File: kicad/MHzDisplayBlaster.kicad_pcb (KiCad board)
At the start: 2 copper layers, 39.6 x 31.2 mm, 5 parts, among them J1 Conn_02x15 DigitRHS, J2 Conn_02x15 DigitLHS, J4 Conn_01x07, U1 DC56-11GWA

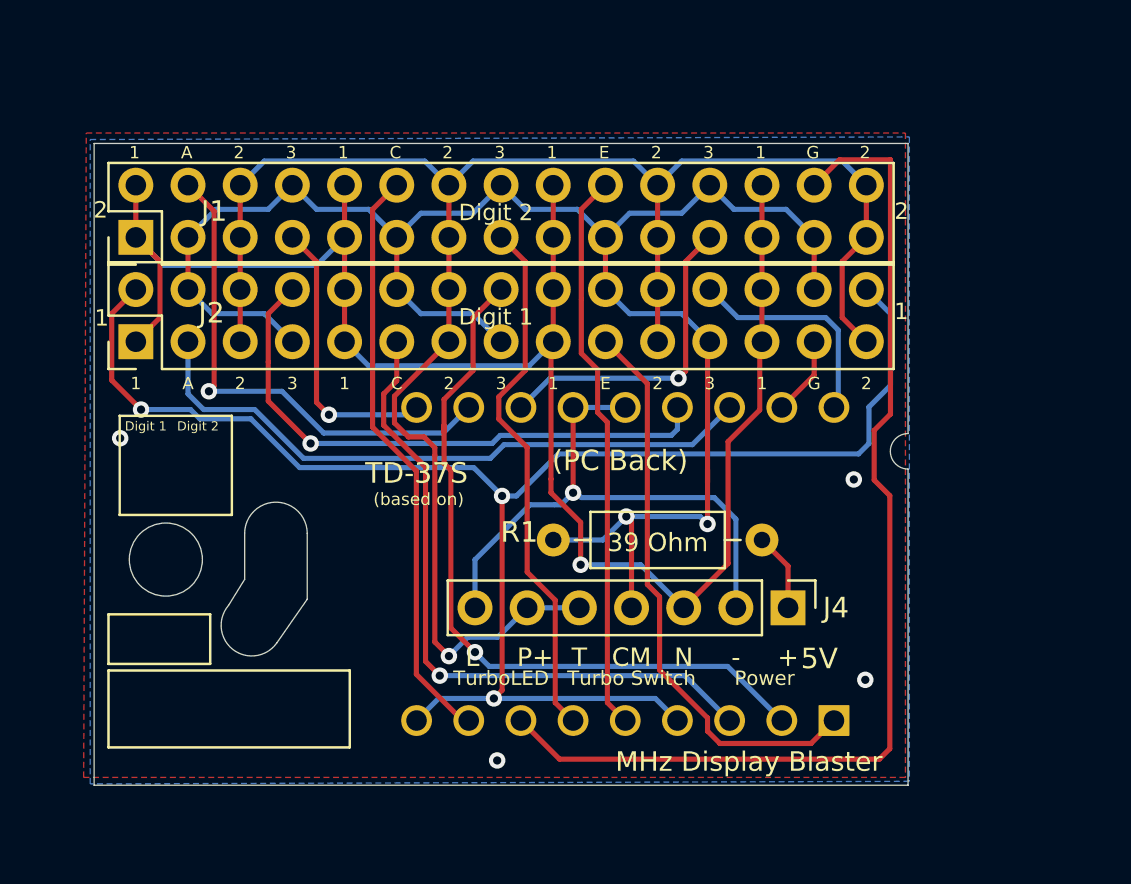
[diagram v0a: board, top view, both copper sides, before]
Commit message: Initial Redesign
Layout rearranged for Gecco labeled Baby AT case. Not even ready as a beta release.
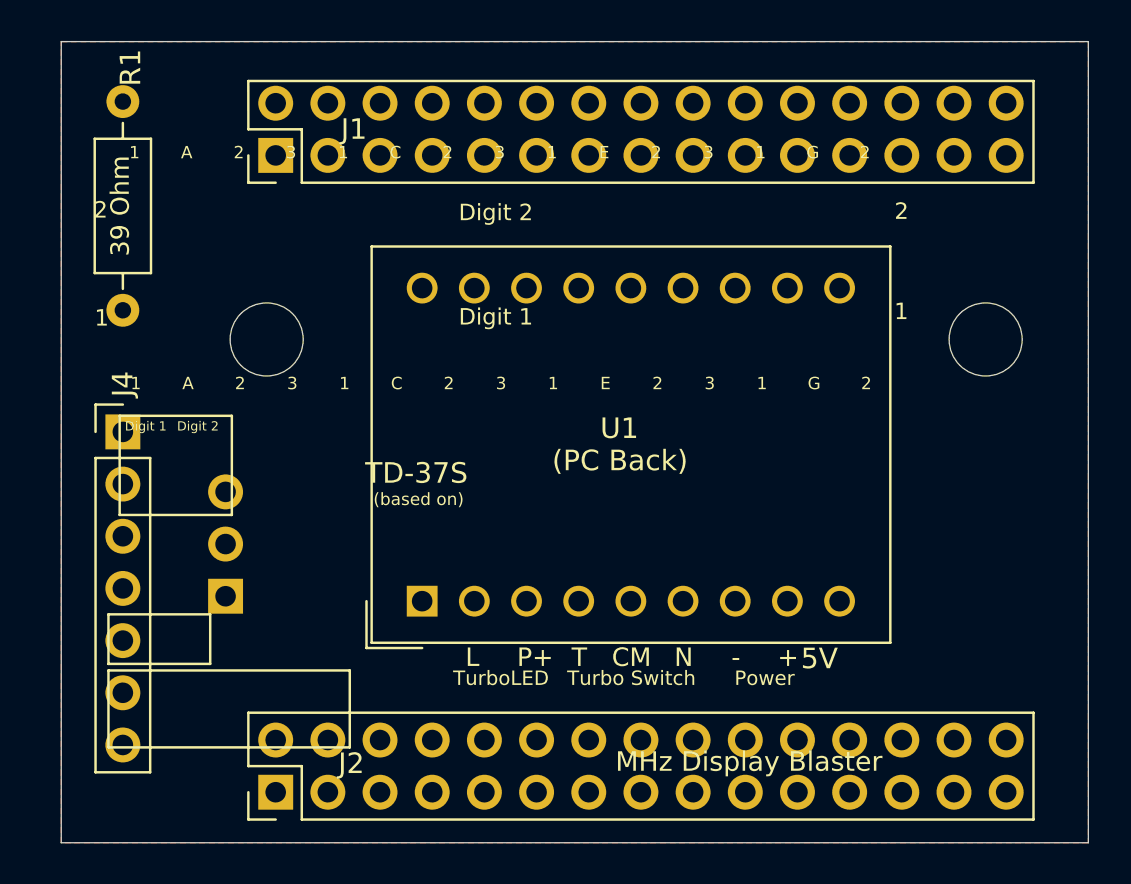
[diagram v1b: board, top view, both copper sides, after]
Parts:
- added J3: Conn_01x03, Connector_PinHeader_2.54mm:PinHeader_1x03_P2.54mm_Vertical, B.Cu at (108.0, 67.0)
- U1: moved to F.Cu
- moved J4 33.5 mm to (103.0, 59.0), turned to 0 degrees
- moved R1 29.9 mm to (103.0, 42.9), turned to -90 degrees
- moved J2 23.0 mm to (110.4, 76.5)
- moved U1 20.9 mm to (117.6, 67.2)
- moved J1 7.89 mm to (110.4, 45.5)
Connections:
- J4 pad 1: Net-(J4-Pad1) -> unconnected-(J4-Pin_1-Pad1)
- R1 pad 2: Net-(J4-Pad1) -> Net-(J3-Pin_2)
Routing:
- net 2: track 90.1 -> 0.00 mm, vias 1 -> 0
- net 3: track 87.6 -> 0.00 mm, vias 6 -> 0
- net 1: track 87.1 -> 0.00 mm, vias 1 -> 0
- net DP: track 77.4 -> 0.00 mm, vias 3 -> 0
- net DIG2_G: track 52.5 -> 0.00 mm
- net DIG1_D: track 36.1 -> 0.00 mm, vias 1 -> 0
- net DIG1_C: track 32.7 -> 0.00 mm, vias 1 -> 0
- net DIG1_A: track 31.2 -> 0.00 mm
- net DIG2_C: track 28.7 -> 0.00 mm
- net DIG1_B: track 28.0 -> 0.00 mm, vias 1 -> 0
- net DIG1_CC: track 27.9 -> 0.00 mm, vias 1 -> 0
- net DIG1_E: track 27.9 -> 0.00 mm
- net DIG2_E: track 27.4 -> 0.00 mm
- net DIG2_D: track 26.0 -> 0.00 mm
- net DIG2_A: track 24.7 -> 0.00 mm, vias 1 -> 0
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- removed copper zone on B.Cu, net 3
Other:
- board size 39.6 x 31.2 mm -> 50 x 39 mm
- net class Default removed

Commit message: Split 7-pin connector
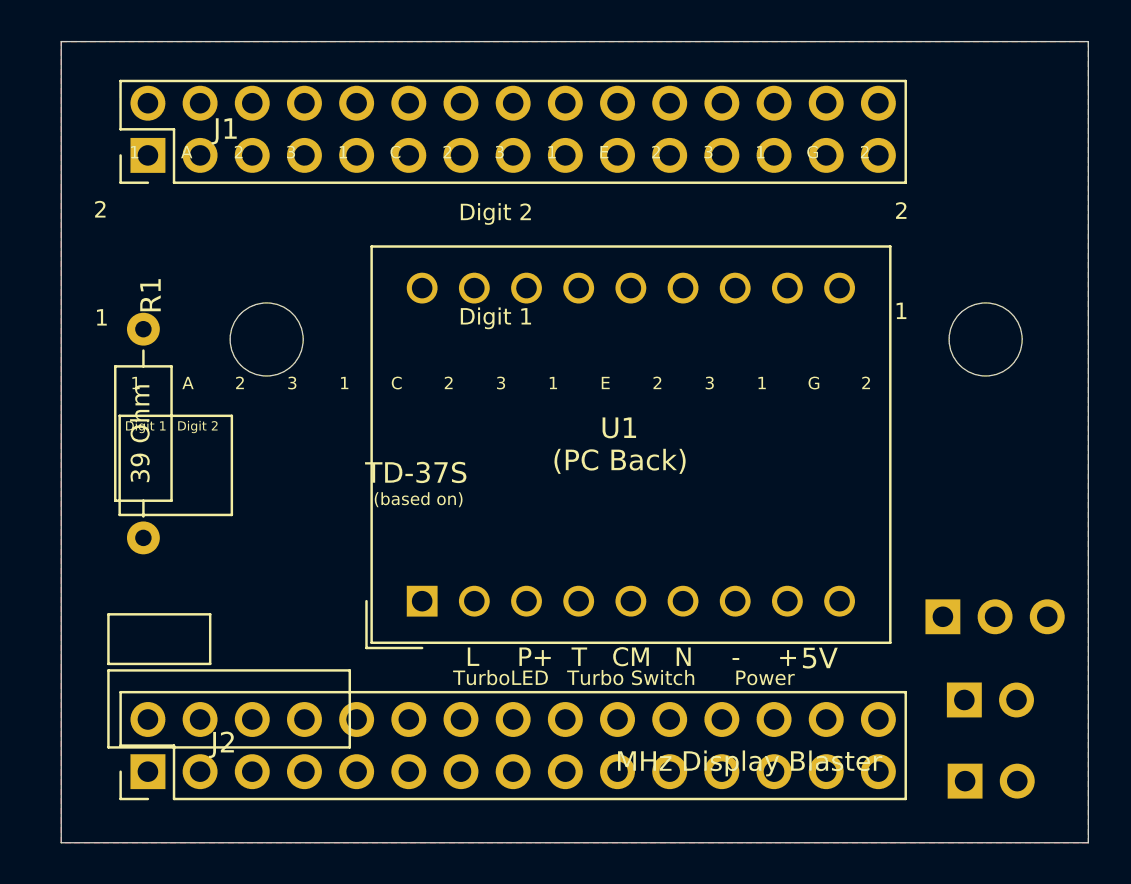
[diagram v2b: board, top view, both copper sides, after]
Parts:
- added J5: Pwr_01x02, Connector_PinHeader_2.54mm:PinHeader_1x02_P2.54mm_Vertical, B.Cu at (144.0, 76.0)
- J3: value Conn_01x03 -> TurboLED_01x02; footprint Connector_PinHeader_2.54mm:PinHeader_1x03_P2.54mm_Vertical -> Connector_PinHeader_2.54mm:PinHeader_1x02_P2.54mm_Vertical
- J4: value Conn_01x07 -> TurboSw_01x03; footprint Connector_PinHeader_2.54mm:PinHeader_1x07_P2.54mm_Vertical -> Connector_PinHeader_2.54mm:PinHeader_1x03_P2.54mm_Vertical; moved to B.Cu
- moved J4 40.9 mm to (142.9, 68.0), turned to -90 degrees
- moved J3 36.3 mm to (144.0, 72.1), turned to -90 degrees
- moved R1 11.1 mm to (104.0, 54.0)
- moved J2 6.30 mm to (104.2, 75.5)
- moved J1 6.22 mm to (104.2, 45.5)
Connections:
- J3 pad 1: unconnected-(J3-Pin_1-Pad1) -> 2
- J3 pad 2: Net-(J3-Pin_2) -> DIG1_CC
- J4 pad 1: unconnected-(J4-Pin_1-Pad1) -> 1
- J4 pad 2: DIG1_CC -> 3
- J4 pad 3: 1 -> 2
- R1 pad 2: Net-(J3-Pin_2) -> Net-(J5-Pin_1)

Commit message: PCB Arrange
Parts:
- moved R1 38.0 mm to (142.0, 53.0)
- moved J4 1.00 mm to (141.9, 68.0)
- moved U1 0.62 mm to (117.0, 67.0)
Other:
- outline, holes or cut-outs redrawn
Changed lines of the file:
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@@
     (property "ki_keywords" "connector")
     (attr through_hole)
-    (fp_text reference "J1" (at 1.27 3.81 180) (layer "F.SilkS")
+    (fp_text reference "J1" (at 1.27 3.81) (layer "F.SilkS")
         (effects (font (size 1 1) (thickness 0.15)))
     )
@@
   )
   (footprint "Display_7Segment:DA56-11CGKWA" locked (layer "F.Cu")
-    (at 117.57 67.24 90)
+    (at 117 67 90)
     (descr "http://www.kingbright.com/attachments/file/psearch/000/00/00/DA56-11CGKWA(Ver.16A).pdf")
     (tags "Double digit seven segment green LED display")
@@
   )
   (footprint "Resistor_THT:R_Axial_DIN0207_L6.3mm_D2.5mm_P10.16mm_Horizontal" (layer "F.Cu")
-    (at 104 54 -90)
+    (at 142 53 -90)
     (descr "Resistor, Axial_DIN0207 series, Axial, Horizontal, pin pitch=10.16mm, 0.25W = 1/4W, length*diameter=6.3*2.5mm^2, http://cdn-reichelt.de/documents/datenblatt/B400/1_4W%23YAG.pdf")
     (tags "Resistor Axial_DIN0207 series Axial Horizontal pin pitch 10.16mm 0.25W = 1/4W length 6.3mm diameter 2.5mm")
@@
   )
   (footprint "Connector_PinHeader_2.54mm:PinHeader_1x03_P2.54mm_Vertical" (layer "B.Cu")
-    (at 142.92 68 -90)
+    (at 141.92 68 -90)
     (descr "Through hole straight pin header, 1x03, 2.54mm pitch, single row")
     (tags "Through hole pin header THT 1x03 2.54mm single row")
@@
   (gr_line (start 100 40) (end 100 79)
     (stroke (width 0.05) (type solid)) (layer "Edge.Cuts"))
-  (gr_circle locked (center 145 54.5) (end 146.778192 54.5)
+  (gr_circle locked (center 146 54) (end 147.5 54)
     (stroke (width 0.05) (type solid)) (fill none) (layer "Edge.Cuts"))
   (gr_line (start 150 40) (end 100 40)
@@
   (gr_line (start 100 79) (end 150 79)
     (stroke (width 0.05) (type solid)) (layer "Edge.Cuts"))
-  (gr_circle locked (center 110 54.5) (end 111.778192 54.5)
+  (gr_circle locked (center 110 54) (end 111.5 54)
     (stroke (width 0.05) (type solid)) (fill none) (layer "Edge.Cuts"))
   (gr_line (start 150 79) (end 150 40)

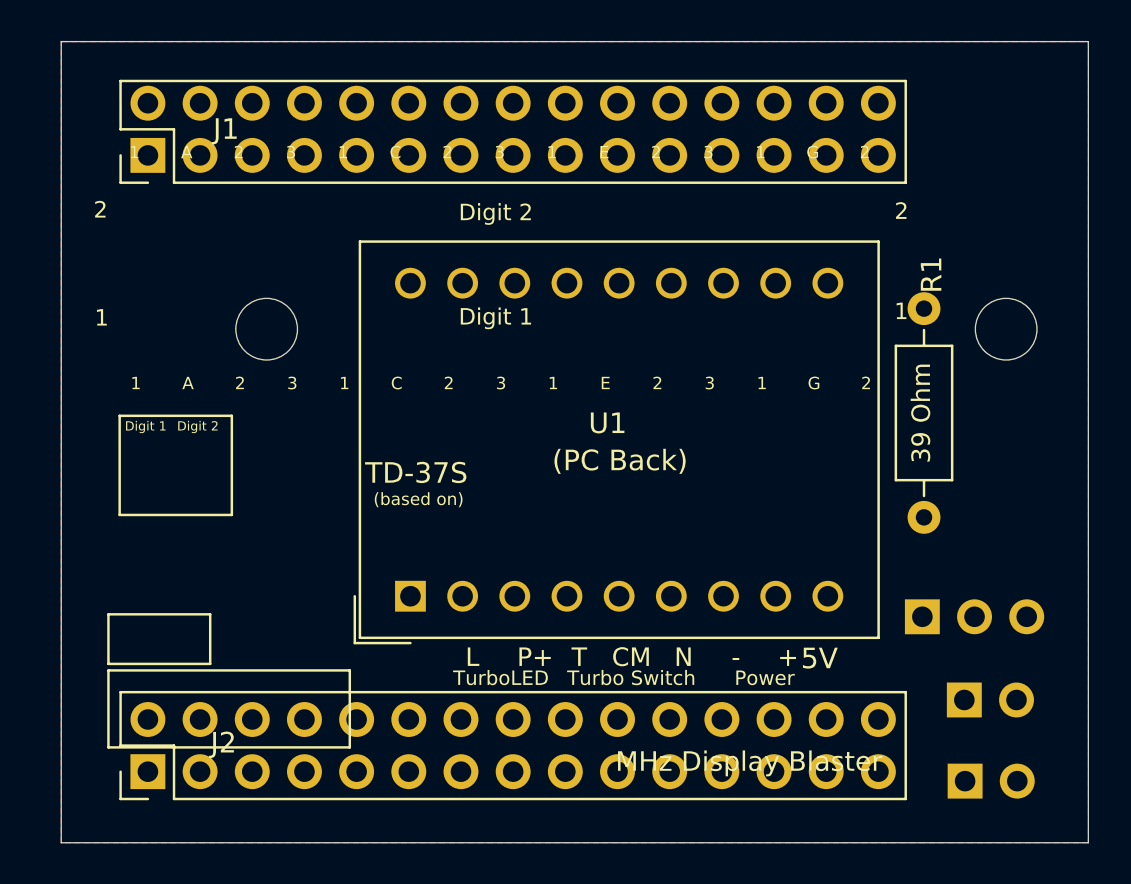
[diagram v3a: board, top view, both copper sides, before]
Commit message: Update Schematic 74LS04
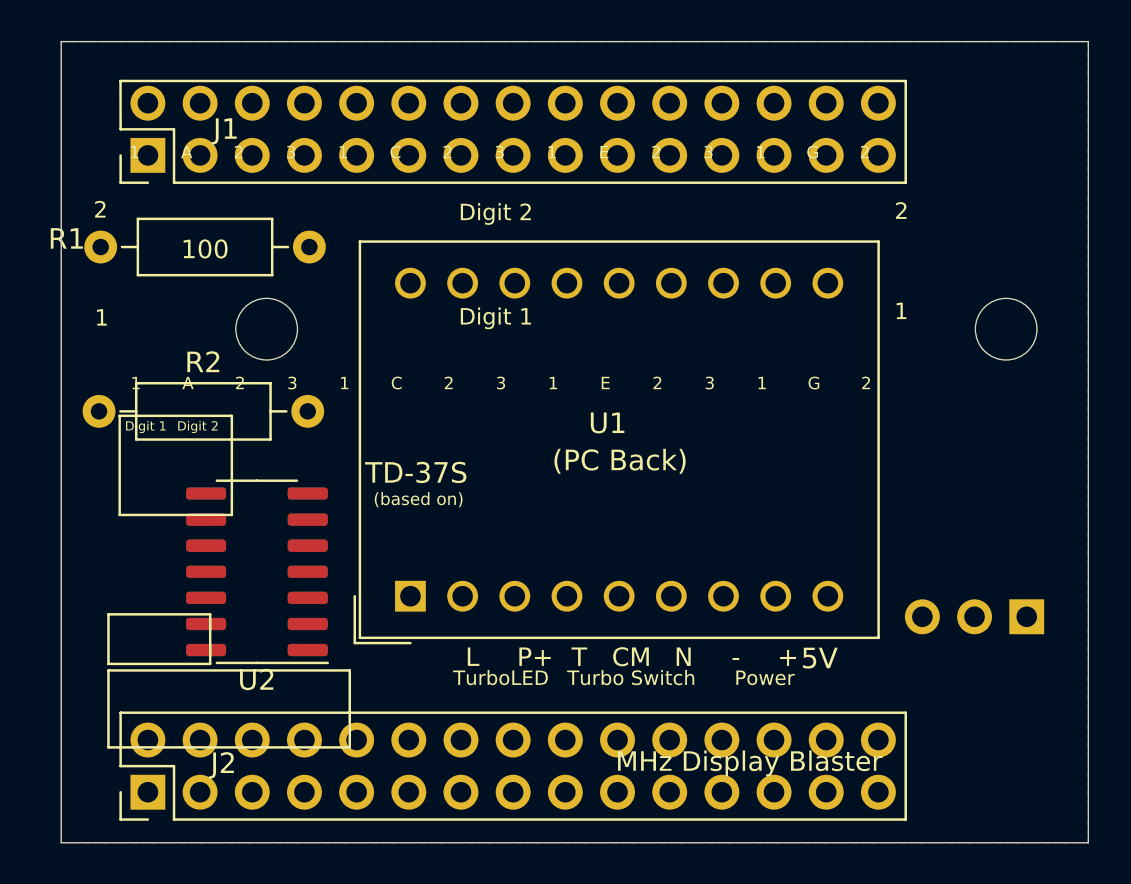
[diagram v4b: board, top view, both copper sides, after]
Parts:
- removed J4: TurboSw_01x03, Connector_PinHeader_2.54mm:PinHeader_1x03_P2.54mm_Vertical
- removed J5: Pwr_01x02, Connector_PinHeader_2.54mm:PinHeader_1x02_P2.54mm_Vertical
- added R2: 1K, Resistor_THT:R_Axial_DIN0207_L6.3mm_D2.5mm_P10.16mm_Horizontal, F.Cu at (101.8, 58.0)
- added U2: 74LS04, Package_SO:SOIC-14_3.9x8.7mm_P1.27mm, F.Cu at (109.5, 65.8)
- J3: value TurboLED_01x02 -> Conn_01x03_Pin; footprint Connector_PinHeader_2.54mm:PinHeader_1x02_P2.54mm_Vertical -> Connector_PinHeader_2.54mm:PinHeader_1x03_P2.54mm_Vertical
- R1: value 39 Ohm -> 100
- moved R1 40.2 mm to (101.9, 50.0), turned to 0 degrees
- moved J3 5.06 mm to (147.0, 68.0), turned to 90 degrees
- moved J2 1.00 mm to (104.2, 76.5)
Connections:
- J3 pad 1: 2 -> Turbo
- J3 pad 2: DIG1_CC -> 3
- R1 pad 1: 3 -> GND
- R1 pad 2: Net-(J5-Pin_1) -> DIG1_CC

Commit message: Cleanup and Routing
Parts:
- R1, R2: footprint Resistor_THT:R_Axial_DIN0207_L6.3mm_D2.5mm_P10.16mm_Horizontal -> Resistor_THT:R_Axial_DIN0204_L3.6mm_D1.6mm_P5.08mm_Horizontal
- moved R1 46.3 mm to (147.5, 58.0), turned to 180 degrees
- moved R2 43.3 mm to (143.0, 71.5), turned to -90 degrees
- moved U2 35.5 mm to (145.0, 64.7)
- moved J1 31.0 mm to (103.4, 45.5)
- moved J2 31.0 mm to (103.8, 76.5)
- moved J3 4.00 mm to (147.0, 72.0), turned to 180 degrees
- renumbered J2 to J1, J1 to J2
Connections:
- J3 pad 1: Turbo -> GND
- J3 pad 3: GND -> Turbo
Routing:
- net 2: track 0.00 -> 143.5 mm
- net 3: track 0.00 -> 143.2 mm
- net 1: track 0.00 -> 137.2 mm
- net DP: track 0.00 -> 76.4 mm
- net DIG2_B: track 0.00 -> 43.1 mm
- net DIG2_A: track 0.00 -> 37.9 mm
- net DIG1_E: track 0.00 -> 30.2 mm
- net DIG1_D: track 0.00 -> 29.6 mm
- net DIG1_C: track 0.00 -> 29.5 mm
- net DIG2_F: track 0.00 -> 26.7 mm
- net DIG2_C: track 0.00 -> 21.4 mm
- net Turbo: track 0.00 -> 20.8 mm
- net DIG1_A: track 0.00 -> 19.8 mm
- net DIG1_G: track 0.00 -> 19.7 mm
- net DIG1_CC: track 0.00 -> 19.4 mm
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- added copper zone on B.Cu, net GND
- removed copper zone on F.Cu, net 3
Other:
- board text added: "+5"
- board text added: "Gnd"
- board text added: "Trbo"
- board text removed: "(PC Back)"
- board text removed: "(PC Front)"
- board text removed: "(based on)"
- board text removed: "+"
- board text removed: "-"
- board text removed: "10"
- board text removed: "18"
- board text removed: "1: Turbo OFF 2: Turbo ON 3: Always ON"
- board text removed: "5V"
- board text removed: "7-Segment Display Common Cathode 0.56""
- board text removed: "B"
- board text removed: "CM"
- board text removed: "D"
- board text removed: "DP"
- board text removed: "Digit 1"
- board text removed: "Digit 2"
- board text removed: "F"
- board text removed: "L"
- board text removed: "N"
- board text removed: "P"
- board text removed: "Power"
- board text removed: "Scrap Computing"
- board text removed: "T"
- board text removed: "TD-37S"
- board text removed: "Turbo Switch"
- board text removed: "TurboLED"
- board text removed: "by Scrap Computing"
- board text removed: "rev.0.2"

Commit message: Small cleanup to text
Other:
- board text removed: "9"
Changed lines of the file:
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@@
   (gr_line (start 150 79) (end 150 40)
     (stroke (width 0.05) (type solid)) (layer "Edge.Cuts"))
-  (gr_text "9" (at 115.171 43.041) (layer "B.SilkS")
-    (effects (font (size 0.6 0.6) (thickness 0.1)) (justify mirror))
-  )
-  (gr_text "1" (at 138.031 43.041) (layer "B.SilkS")
-    (effects (font (size 0.6 0.6) (thickness 0.1)) (justify mirror))
-  )
   (gr_text "Trbo" (at 145.67 77) (layer "B.SilkS")
     (effects (font (size 0.5 0.5) (thickness 0.125)) (justify left bottom mirror))

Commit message: Remove ground plane
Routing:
- net GND: track 2.91 -> 17.1 mm
- removed copper zone on B.Cu, net GND
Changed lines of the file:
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@@
   (segment (start 147.54 58) (end 147.5064 58.0336) (width 0.25) (layer "F.Cu") (net 21))
   (segment (start 147.5064 58.0336) (end 147.5064 60.8925) (width 0.25) (layer "F.Cu") (net 21))
+  (segment (start 147 58.54) (end 147.54 58) (width 0.25) (layer "B.Cu") (net 21))
+  (segment (start 147 72) (end 147 58.54) (width 0.25) (layer "B.Cu") (net 21))
   (zone (net 0) (net_name "") (layer "F.Cu") (hatch edge 0.508)
     (connect_pads (clearance 0))
@@
       )
     )
-  )
-  (zone (net 21) (net_name "GND") (layer "B.Cu") (hatch edge 0.508)
-    (connect_pads (clearance 0))
-    (min_thickness 0.254) (filled_areas_thickness no)
-    (fill yes (thermal_gap 0.508) (thermal_bridge_width 0.508) (island_removal_mode 1) (island_area_min 10))
-    (polygon
-      (pts
-        (xy 141 57)
-        (xy 149 57)
-        (xy 149 78)
-        (xy 141 78)
-      )
-    )

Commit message: Major Refactor and Cleanup
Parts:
- R1, U2: moved to B.Cu
- moved R1 15.2 mm to (143.0, 43.5), turned to -90 degrees
- moved R2 5.68 mm to (147.5, 68.0), turned to 180 degrees
- moved U2 2.89 mm to (145.0, 61.8), turned to 0 degrees
- moved J3 2.69 mm to (148.0, 74.5), turned to 90 degrees
- moved J2 0.32 mm to (103.4, 76.5)
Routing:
- net GND: track 17.1 -> 0.00 mm, vias 0 -> 5
- net DP: track 76.4 -> 61.8 mm
- net 3: track 143.2 -> 129.6 mm
- net 2: track 143.5 -> 132.5 mm
- net 1: track 137.2 -> 147.0 mm
- net DIG1_C: track 29.5 -> 24.5 mm, vias 0 -> 1
- net DIG1_E: track 30.2 -> 25.5 mm, vias 0 -> 2
- net DIG2_A: track 37.9 -> 42.1 mm
- net DIG2_C: track 21.4 -> 24.3 mm, vias 0 -> 1
- net DIG1_CC: track 19.4 -> 17.3 mm
- net DIG1_A: track 19.8 -> 18.7 mm
- net DIG1_D: track 29.6 -> 28.7 mm
- net Turbo: track 20.8 -> 20.2 mm
- net DIG2_F: track 26.7 -> 26.1 mm
- net DIG1_F: track 18.7 -> 19.0 mm, vias 0 -> 1
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- added copper zone on B.Cu, net GND
- added copper zone on F.Cu, net GND
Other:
- board text added: "Trb"
- board text removed: "Trbo"
